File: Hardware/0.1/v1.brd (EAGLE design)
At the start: 75.9 x 67.3 mm, 23 parts, among them K1 ZF112, K2 ZF112, K3 ZF112, K4 ZF112

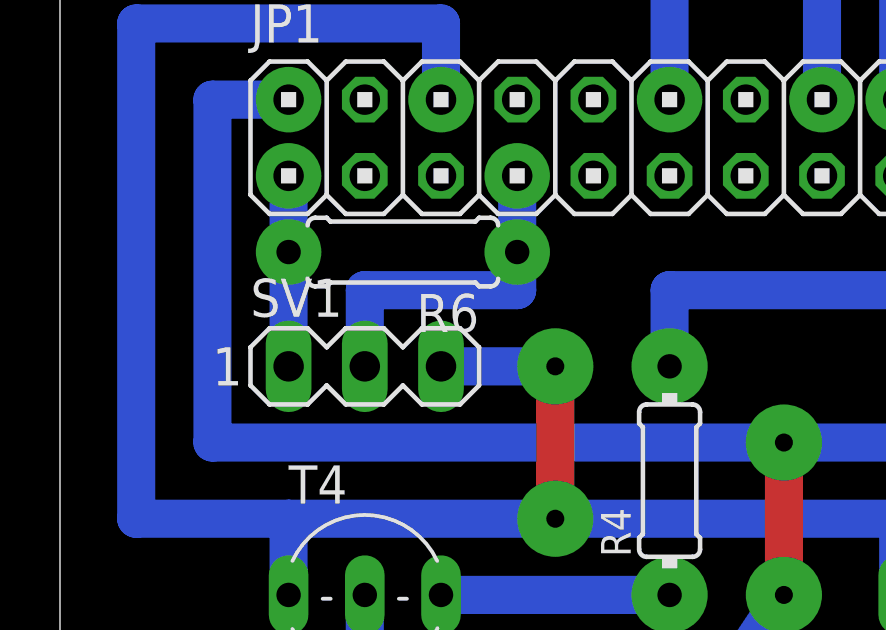
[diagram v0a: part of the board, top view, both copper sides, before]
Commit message: wartości na schemacie
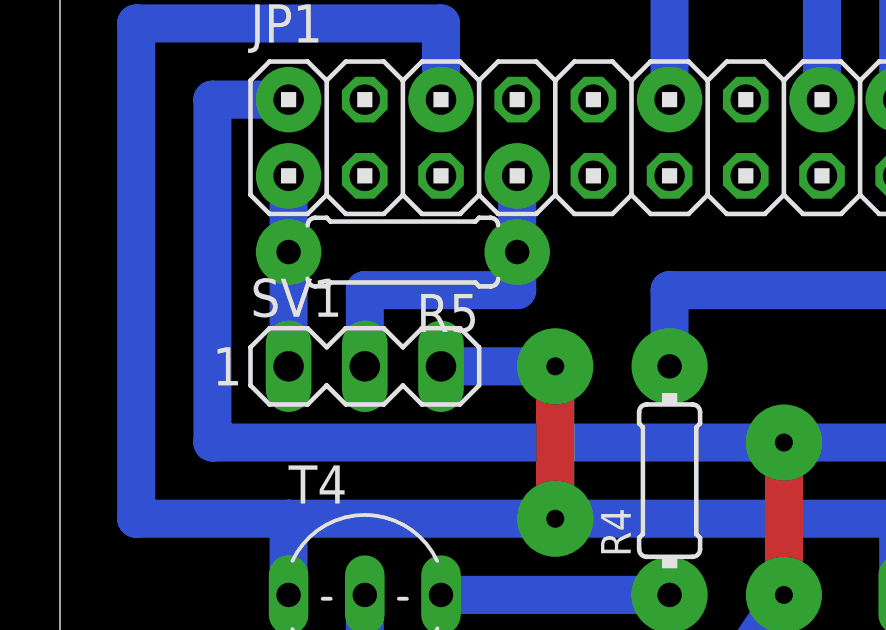
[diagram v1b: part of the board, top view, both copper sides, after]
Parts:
- R1, R2, R3, R4, R5: value (none) -> 4,7k
- renumbered R6 to R5
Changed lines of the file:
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@@
 <?xml version="1.0" encoding="utf-8"?>
 <!DOCTYPE eagle SYSTEM "eagle.dtd">
-<eagle version="6.2">
+<eagle version="6.1">
 <drawing>
 <settings>
@@
 </element>
 <element name="JP1" library="pinhead" package="2X13" value="" x="20.32" y="57.15"/>
-<element name="R1" library="rcl" package="0204/7" value="" x="63.5" y="45.72" rot="R90"/>
-<element name="R2" library="rcl" package="0204/7" value="" x="48.26" y="45.72" rot="R90"/>
+<element name="R1" library="rcl" package="0204/7" value="4,7k" x="63.5" y="45.72" rot="R90"/>
+<element name="R2" library="rcl" package="0204/7" value="4,7k" x="48.26" y="45.72" rot="R90"/>
 <element name="K3" library="relay" package="ZF112" value="ZF112" x="60.96" y="21.59" rot="R270">
 <attribute name="OC_NEWARK" value="unknown" x="60.96" y="21.59" size="1.778" layer="27" rot="R270" display="off"/>
@@
 <attribute name="OC_FARNELL" value="unknown" x="35.56" y="-6.35" size="1.778" layer="27" rot="R180" display="off"/>
 </element>
-<element name="R3" library="rcl" package="0204/7" value="" x="33.02" y="45.72" rot="R90"/>
+<element name="R3" library="rcl" package="0204/7" value="4,7k" x="33.02" y="45.72" rot="R90"/>
 <element name="K2" library="relay" package="ZF112" value="ZF112" x="27.94" y="21.59" rot="R270">
 <attribute name="OC_NEWARK" value="unknown" x="3.81" y="30.48" size="1.778" layer="27" rot="R270" display="off"/>
@@
 <attribute name="OC_FARNELL" value="unknown" x="19.05" y="-6.35" size="1.778" layer="27" rot="R180" display="off"/>
 </element>
-<element name="R4" library="rcl" package="0204/7" value="" x="17.78" y="45.72" rot="R90"/>
+<element name="R4" library="rcl" package="0204/7" value="4,7k" x="17.78" y="45.72" rot="R90"/>
 <element name="K4" library="relay" package="ZF112" value="ZF112" x="11.43" y="21.59" rot="R270">
 <attribute name="OC_NEWARK" value="unknown" x="-12.7" y="30.48" size="1.778" layer="27" rot="R270" display="off"/>
@@
 <attribute name="OC_FARNELL" value="unknown" x="7.62" y="49.53" size="1.778" layer="27" display="off"/>
 </element>
-<element name="R6" library="rcl" package="0207/7" value="" x="8.89" y="53.34" rot="R180"/>
+<element name="R5" library="rcl" package="0207/7" value="4,7k" x="8.89" y="53.34" rot="R180"/>
 </elements>
 <signals>
@@
 <contactref element="SV1" pad="1"/>
 <wire x1="5.08" y1="49.53" x2="5.08" y2="55.88" width="1.27" layer="16"/>
-<contactref element="R6" pad="2"/>
+<contactref element="R5" pad="2"/>
 <wire x1="5.08" y1="55.88" x2="5.08" y2="53.34" width="0" layer="19" extent="1-1"/>
 </signal>
@@
 <wire x1="12.7" y1="52.07" x2="7.62" y2="52.07" width="1.27" layer="16"/>
 <wire x1="7.62" y1="52.07" x2="7.62" y2="49.53" width="1.27" layer="16"/>
-<contactref element="R6" pad="1"/>
+<contactref element="R5" pad="1"/>
 <wire x1="12.7" y1="52.07" x2="12.7" y2="53.34" width="0" layer="19" extent="16-16"/>
 </signal>

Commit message: dopisane kolejne wartości
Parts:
- D1, D2, D3, D4: value 1N4004 -> 1N4148
- K1, K2, K3, K4: value ZF112 -> SRD-5VDC-SL-C
- R1, R2, R3, R4: value 4,7k -> 470
- T1, T2, T3, T4: value (none) -> BC639
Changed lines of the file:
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@@
 </autorouter>
 <elements>
-<element name="D1" library="diode" package="DO41-10" value="1N4004" x="60.96" y="36.83" rot="R180"/>
-<element name="T1" library="transistor" package="TO92-ECB" value="" x="58.42" y="41.91"/>
+<element name="D1" library="diode" package="DO41-10" value="1N4148" x="60.96" y="36.83" rot="R180"/>
+<element name="T1" library="transistor" package="TO92-ECB" value="BC639" x="58.42" y="41.91"/>
 <element name="X1" library="con-wago-500" package="W237-103" value="" x="60.96" y="3.81" rot="R180">
 <attribute name="OC_NEWARK" value="18M7116" x="60.96" y="3.81" size="1.778" layer="27" rot="R180" display="off"/>
@@
 <attribute name="OC_FARNELL" value="unknown" x="60.96" y="3.81" size="1.778" layer="27" rot="R180" display="off"/>
 </element>
-<element name="D2" library="diode" package="DO41-10" value="1N4004" x="44.45" y="36.83" rot="R180"/>
-<element name="T2" library="transistor" package="TO92-ECB" value="" x="43.18" y="41.91"/>
+<element name="D2" library="diode" package="DO41-10" value="1N4148" x="44.45" y="36.83" rot="R180"/>
+<element name="T2" library="transistor" package="TO92-ECB" value="BC639" x="43.18" y="41.91"/>
 <element name="X3" library="con-wago-500" package="W237-103" value="" x="44.45" y="3.81" rot="R180">
 <attribute name="OC_NEWARK" value="18M7116" x="52.07" y="15.24" size="1.778" layer="27" rot="R180" display="off"/>
@@
 </element>
 <element name="JP1" library="pinhead" package="2X13" value="" x="20.32" y="57.15"/>
-<element name="R1" library="rcl" package="0204/7" value="4,7k" x="63.5" y="45.72" rot="R90"/>
-<element name="R2" library="rcl" package="0204/7" value="4,7k" x="48.26" y="45.72" rot="R90"/>
-<element name="K3" library="relay" package="ZF112" value="ZF112" x="60.96" y="21.59" rot="R270">
+<element name="R1" library="rcl" package="0204/7" value="470" x="63.5" y="45.72" rot="R90"/>
+<element name="R2" library="rcl" package="0204/7" value="470" x="48.26" y="45.72" rot="R90"/>
+<element name="K3" library="relay" package="ZF112" value="SRD-5VDC-SL-C" x="60.96" y="21.59" rot="R270">
 <attribute name="OC_NEWARK" value="unknown" x="60.96" y="21.59" size="1.778" layer="27" rot="R270" display="off"/>
 <attribute name="MPN" value="" x="60.96" y="21.59" size="1.778" layer="27" rot="R270" display="off"/>
@@
 <attribute name="OC_FARNELL" value="unknown" x="60.96" y="21.59" size="1.778" layer="27" rot="R270" display="off"/>
 </element>
-<element name="K1" library="relay" package="ZF112" value="ZF112" x="44.45" y="21.59" rot="R270">
+<element name="K1" library="relay" package="ZF112" value="SRD-5VDC-SL-C" x="44.45" y="21.59" rot="R270">
 <attribute name="OC_NEWARK" value="unknown" x="44.45" y="21.59" size="1.778" layer="27" rot="R270" display="off"/>
 <attribute name="MPN" value="" x="44.45" y="21.59" size="1.778" layer="27" rot="R270" display="off"/>
@@
 <attribute name="OC_FARNELL" value="unknown" x="44.45" y="21.59" size="1.778" layer="27" rot="R270" display="off"/>
 </element>
-<element name="D3" library="diode" package="DO41-10" value="1N4004" x="27.94" y="36.83" rot="R180"/>
-<element name="T3" library="transistor" package="TO92-ECB" value="" x="27.94" y="41.91"/>
+<element name="D3" library="diode" package="DO41-10" value="1N4148" x="27.94" y="36.83" rot="R180"/>
+<element name="T3" library="transistor" package="TO92-ECB" value="BC639" x="27.94" y="41.91"/>
 <element name="X2" library="con-wago-500" package="W237-103" value="" x="27.94" y="3.81" rot="R180">
 <attribute name="OC_NEWARK" value="18M7116" x="35.56" y="-6.35" size="1.778" layer="27" rot="R180" display="off"/>
@@
 <attribute name="OC_FARNELL" value="unknown" x="35.56" y="-6.35" size="1.778" layer="27" rot="R180" display="off"/>
 </element>
-<element name="R3" library="rcl" package="0204/7" value="4,7k" x="33.02" y="45.72" rot="R90"/>
-<element name="K2" library="relay" package="ZF112" value="ZF112" x="27.94" y="21.59" rot="R270">
+<element name="R3" library="rcl" package="0204/7" value="470" x="33.02" y="45.72" rot="R90"/>
+<element name="K2" library="relay" package="ZF112" value="SRD-5VDC-SL-C" x="27.94" y="21.59" rot="R270">
 <attribute name="OC_NEWARK" value="unknown" x="3.81" y="30.48" size="1.778" layer="27" rot="R270" display="off"/>
 <attribute name="MPN" value="" x="3.81" y="30.48" size="1.778" layer="27" rot="R270" display="off"/>
@@
 <attribute name="OC_FARNELL" value="unknown" x="3.81" y="30.48" size="1.778" layer="27" rot="R270" display="off"/>
 </element>
-<element name="D4" library="diode" package="DO41-10" value="1N4004" x="11.43" y="36.83" rot="R180"/>
-<element name="T4" library="transistor" package="TO92-ECB" value="" x="7.62" y="41.91"/>
+<element name="D4" library="diode" package="DO41-10" value="1N4148" x="11.43" y="36.83" rot="R180"/>
+<element name="T4" library="transistor" package="TO92-ECB" value="BC639" x="7.62" y="41.91"/>
 <element name="X4" library="con-wago-500" package="W237-103" value="" x="11.43" y="3.81" rot="R180">
 <attribute name="OC_NEWARK" value="18M7116" x="19.05" y="-6.35" size="1.778" layer="27" rot="R180" display="off"/>
@@
 <attribute name="OC_FARNELL" value="unknown" x="19.05" y="-6.35" size="1.778" layer="27" rot="R180" display="off"/>
 </element>
-<element name="R4" library="rcl" package="0204/7" value="4,7k" x="17.78" y="45.72" rot="R90"/>
-<element name="K4" library="relay" package="ZF112" value="ZF112" x="11.43" y="21.59" rot="R270">
+<element name="R4" library="rcl" package="0204/7" value="470" x="17.78" y="45.72" rot="R90"/>
+<element name="K4" library="relay" package="ZF112" value="SRD-5VDC-SL-C" x="11.43" y="21.59" rot="R270">
 <attribute name="OC_NEWARK" value="unknown" x="-12.7" y="30.48" size="1.778" layer="27" rot="R270" display="off"/>
 <attribute name="MPN" value="" x="-12.7" y="30.48" size="1.778" layer="27" rot="R270" display="off"/>
